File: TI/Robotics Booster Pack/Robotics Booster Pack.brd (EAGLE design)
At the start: 68.6 x 76.2 mm, 115 parts, among them J1 1X2.PTS, U1 TS3A44159.RGT, U10 74LVTH125.RGY, U11 SCHA4B0400, U12 BLUETOOTH-RN41", U13 XBEE-1XBEE-1_LOCK, U14 TPS5450, U15 TPS715XX.DCK, U16 TPS62152.RGT, U3 DRV8800, U4 DRV8800, U5 DRV8800, U6 DRV8800, U7 PCA9557.RGV, U8 MPU-6050, U9 INA220.DGS

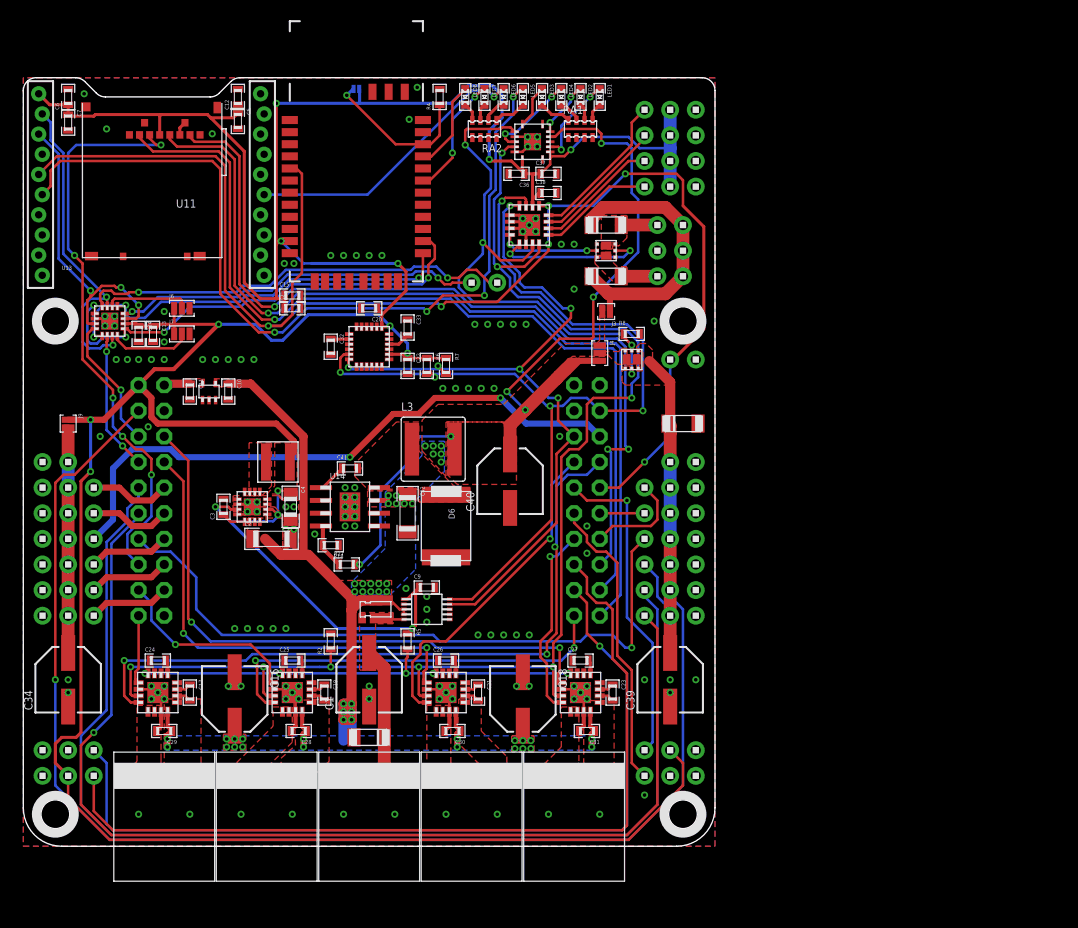
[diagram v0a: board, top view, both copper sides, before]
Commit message: Began starting on v2.1 Removed: Bluetooth Module, Servo Enable IC, Buffer IC. Corrected Motor PWM/IO signals issue Centered power ICs
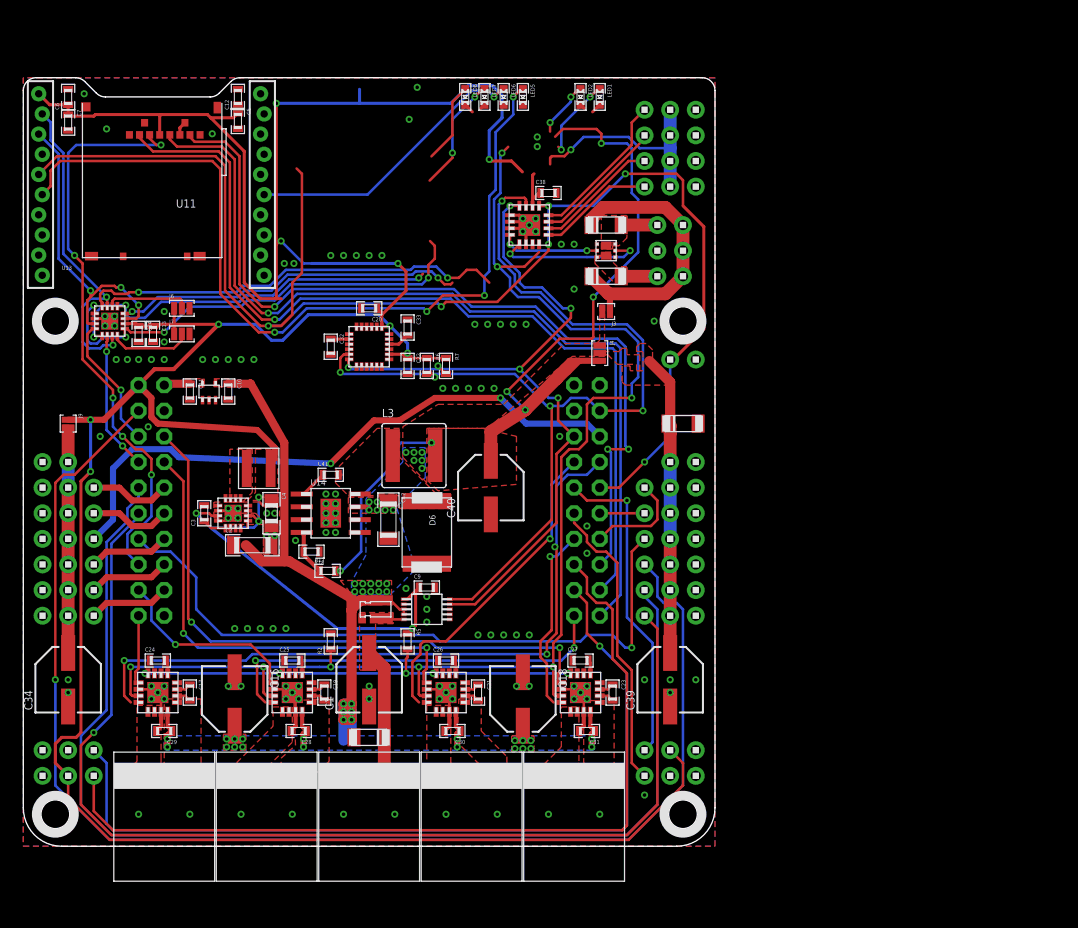
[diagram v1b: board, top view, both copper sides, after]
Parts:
- removed C15, C37: 1uF, standardparts:0603
- removed C36, C8: .1uF, standardparts:0603
- removed J2: (no value), solderjumper:2.MED
- removed LED3, LED4: (no value), standardparts:0603.LED
- removed Q2: (no value), fairchild:MICROFET.2X2
- removed R4: 1k, standardparts:0603
- removed R8: 10k, standardparts:0603
- removed RA1, RA2: 1k, resistorarray:0603.4.C
- removed U$15: 1X2, headers(.1in):1X2
- removed U10: 74LVTH125.RGY, packages(ti):RGY.14
- removed U12: BLUETOOTH-RN41", SparkFun-RF:RN41
- moved C42 2.01 mm to (36.2, 32.4)
- moved R17 2.01 mm to (30.2, 27.3)
- moved C3 2.01 mm to (17.9, 33.0)
- moved C4 2.01 mm to (24.6, 33.0)
- moved C40 2.01 mm to (46.4, 35.6)
- moved L1 2.01 mm to (23.3, 37.5)
- moved L3 2.01 mm to (38.7, 38.7)
- moved R18 2.01 mm to (28.6, 29.2)
- moved U16 2.01 mm to (20.8, 33.0)
- moved C41 2.01 mm to (30.5, 36.8)
- moved C2 2.01 mm to (22.7, 29.8)
- moved U14 2.01 mm to (30.5, 33.0)
- moved D6 2.01 mm to (40.0, 31.1)
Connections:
- removed net BT.RESET: J2.1, R4.1, U12.22
- removed net N$12: LED4.P$2, RA1.4
- removed net N$15: LED6.P$2, RA2.3
- removed net N$16: J4.2, Q2.3, Q2.6, Q2.PAD@1, Q2.PAD@2
- removed net N$17: LED5.P$2, RA2.1
- removed net N$26: LED3.P$2, RA1.2
- removed net N$32: LED3.P$1, U10.8
- removed net N$6: LED4.P$1, U10.11
- removed net SRVO.EN: Q2.2, Q2.5, R8.1, U10.9, U7.7
- new net VDD: J4.2
- net !RST: no longer U12.5
- net 3.3V: no longer C15.1, C36.1, C37.1, C8.1, J2.2, U10.14, U10.2, U12.11
- net 5.0V: no longer U10.5
- net BT.CONNECT: no longer U12.21
- net BT.RXI: no longer U12.14
- net BT.STATUS: no longer U12.19
- net BT.TXO: no longer U12.13
- net GND: no longer C15.2, C36.2, C37.2, C8.2, R4.2, R8.2, RA1.1, RA1.3, RA1.5, RA1.7, RA2.2, RA2.4, RA2.6, RA2.8, U10.1, U10.10, U10.13, U10.4, U10.7, U10.PAD, U12.1, U12.12, U12.25, U12.27, U12.28, U12.29
- net M.EN: no longer U10.12, U7.8
- net M0.DIR: now also U5.1; no longer U5.4
- net M0.SPD: now also U5.4; no longer U5.1
- net M1.DIR: now also U6.1; no longer U6.4
- net M1.SPD: now also U6.4; no longer U6.1
- net M2.DIR: now also U3.1; no longer U3.4
- net M2.SPD: now also U3.4; no longer U3.1
- net M3.DIR: now also U4.1; no longer U4.4
- net M3.SPD: now also U4.4; no longer U4.1
- net N$10: no longer U10.6
- net N$11: no longer U10.3
- net N$14: no longer RA2.7
- net N$5: no longer RA1.8
- net N$8: no longer RA1.6
- net N$9: no longer RA2.5
- net UART0.RXI: no longer U$15.2
- net UART0.TXO: no longer U$15.1
- net VSERVO: no longer Q2.1, Q2.4
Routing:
- net SRVO.EN: track 54.7 -> 0.00 mm, vias 4 -> 0
- net BT.RESET: track 15.6 -> 0.00 mm, vias 1 -> 0
- net N$6: track 8.94 -> 0.00 mm, vias 2 -> 0
- net 3.3V: track 388.9 -> 380.3 mm
- net N$32: track 4.27 -> 0.00 mm
- net N$26: track 3.26 -> 0.00 mm
- net N$17: track 3.25 -> 0.00 mm
- net GND: track 40.4 -> 37.6 mm, vias 132 -> 130
- net N$15: track 2.44 -> 0.00 mm
- net N$12: track 2.35 -> 0.00 mm
- net BT.TXO: track 42.0 -> 39.9 mm
- net UART0.TXO: track 36.7 -> 34.8 mm
- net M.EN: track 133.0 -> 131.6 mm
- net 5.0V: track 83.0 -> 84.5 mm
- net N$9: track 1.72 -> 0.57 mm
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
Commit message: Let the carnage that shall be known as v3 begin!
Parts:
- removed C10, C13: .1uF, standardparts:0603
- removed C11, C14: 1uF, standardparts:0603
- removed D5: CDBMT2100-HF, comchip:SOD-123H
- removed H11, H12: 1X4, headers(.1in):1X4
- removed H17, H18, H19, H20, J1: 1X2.PTS, phoenixcontact:PTS.PLUG
- removed J6, J7: (no value), solderjumper:3.LRG
- removed J9: (no value), solderjumper:2.LRG.PASTE
- removed R2: 10k, standardparts:0603
- removed U$11, U$14: HOLE.4MM, screw_holes:4MM
- removed U1: TS3A44159.RGT, packages(ti):RGT.16
- removed U15: TPS715XX.DCK, packages(ti):DCK
- added H8: 1X4.182440000, weidmuller:1824440000
- H1, H2, H4, H5: value 1X7 -> 1X6; device headers(.1in):1X7 -> headers(.1in):1X6
- H10: value 1X4 -> 1X4.182440000; device headers(.1in):1X4 -> weidmuller:1824440000
- moved C6 107.7 mm to (89.5, 8.26), turned to 270 degrees
- moved C7 104.7 mm to (89.5, 10.8), turned to 90 degrees
- moved U11 84.7 mm to (74.3, 8.89), turned to 0 degrees
- moved C12 83.7 mm to (72.7, 8.26), turned to 270 degrees
- moved C5 80.0 mm to (72.7, 10.6), turned to 90 degrees
- moved U13 73.6 mm to (81.3, 27.9), turned to 180 degrees
- moved C23 58.2 mm to (31.1, 66.7), turned to 0 degrees
- moved C31 56.7 mm to (34.9, 64.1), turned to 270 degrees
- moved U4 54.0 mm to (31.1, 63.5), turned to 90 degrees
- moved C27 52.7 mm to (27.9, 63.5), turned to 90 degrees
- moved C18 46.7 mm to (31.8, 57.8), turned to 0 degrees
- moved C40 46.6 mm to (5.08, 57.1), turned to 270 degrees
- moved LED1 45.1 mm to (85.7, 39.4)
- moved LED2 45.1 mm to (83.8, 39.4)
- moved LED5 45.1 mm to (78.1, 39.4)
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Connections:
- removed net BT.CONNECT: LED8.P$1
- removed net BT.RXI: U1.13, U1.5
- removed net BT.STATUS: LED7.P$1
- removed net BT.TXO: U1.1, U1.9
- removed net IO0: H12.1, U7.12
- removed net IO1: H12.2, U7.11
- removed net IO2: H12.3, U7.10
- removed net IO3: H12.4, U7.9
- removed net M.EN: R2.1, U3.3, U4.3, U5.3, U6.3
- removed net N$2: J6.2, U1.2
- removed net N$3: J7.2, U1.12
- removed net UART0.RXI: U1.4
- removed net UART0.TXO: U1.16
- removed net VBUS: C11.1, U$8.VBUS, U15.5
- new net IMU.INT: U7.5, U8.12
- new net M0.EN: U5.3, U7.9
- new net M1.EN: U6.3, U7.10
- new net M2.EN: U3.3, U7.11
- new net M3.EN: U4.3, U7.12
- new net XBEE.CONNECTED: U13.17, U7.4
- net 3.3V: no longer C13.1, C14.1, H11.1, H11.2, H11.3, H11.4, J6.1, J7.1, J9.1, U1.14
- net 5.0V: now also U$8.VBUS
- net FET0.G: now also U7.7; no longer U7.4
- net FET1.G: now also U7.8; no longer U7.5
- net GND: no longer C10.2, C11.2, C13.2, C14.2, D5.2, H1.7, H10.1, H10.2, H10.3, H10.4, H4.7, J1.2, J6.3, J7.3, R2.2, U1.6, U1.PAD, U15.2
- net M0+: now also H8.1@1, H8.1@2; no longer H17.1
- net M0-: now also H8.2@1, H8.2@2; no longer H17.2
- net M0.DIR: now also U$8.PC4; no longer U$8.PF0
- net M1+: now also H8.3@1, H8.3@2; no longer H18.1
- net M1-: now also H8.4@1, H8.4@2; no longer H18.2
- net M1.DIR: now also U$8.PC7; no longer U$8.PF4
- net M2+: now also H10.1@1, H10.1@2; no longer H19.1
- net M2-: now also H10.2@1, H10.2@2; no longer H19.2
- net M2.DIR: now also U$8.PF0; no longer U$8.PC4
- net M3+: now also H10.3@1, H10.3@2; no longer H20.1
- net M3-: now also H10.4@1, H10.4@2; no longer H20.2
- net M3.DIR: now also U$8.PF4; no longer U$8.PC7
- net N$22: no longer J1.1
- net N$4: no longer H5.7, J9.2
- net UART1.RXI: no longer U1.8
- net UART1.TXO: no longer U1.10
- net VBAT: no longer C10.1, U15.4
- net VSERVO: no longer D5.1, H2.7
- net XBEE.RXI: no longer U1.11, U1.3
- net XBEE.TXO: no longer U1.15, U1.7
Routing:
- net 3.3V: track 380.3 -> 3.81 mm, vias 14 -> 0
- net !RST: track 144.0 -> 0.00 mm, vias 6 -> 0
- net SVRO3: track 132.1 -> 0.00 mm, vias 1 -> 0
- net M.EN: track 131.6 -> 0.00 mm, vias 8 -> 0
- net SVRO4: track 115.2 -> 0.00 mm
- net SVRO5: track 110.2 -> 0.00 mm, vias 1 -> 0
- net I2C.SCL: track 95.1 -> 0.00 mm, vias 5 -> 0
- net SPI.SCLK: track 90.0 -> 0.00 mm, vias 1 -> 0
- net SPI.!CS: track 89.6 -> 0.00 mm, vias 1 -> 0
- net QEI0.A: track 85.9 -> 0.00 mm
- net QEI0.B: track 85.4 -> 0.00 mm, vias 1 -> 0
- net SPI.MISO: track 85.3 -> 0.00 mm, vias 3 -> 0
- net XBEE.RSSI: track 84.3 -> 0.00 mm, vias 4 -> 0
- net VBAT: track 81.8 -> 1.20 mm, vias 48 -> 12
- net I2C.SDA: track 75.9 -> 0.00 mm, vias 6 -> 0
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- added copper zone on layer 16, net 3.3V
- added copper zone on layer 16, net N$1
- removed copper zone on layer 1, net 3.3V
- removed copper zone on layer 1, net 5.0V
- removed copper zone on layer 1, net M0+
- removed copper zone on layer 1, net M0-
- removed copper zone on layer 1, net M1+
- removed copper zone on layer 1, net M1-
- removed copper zone on layer 1, net M2+
- removed copper zone on layer 1, net M2-
- removed copper zone on layer 1, net M3+
- removed copper zone on layer 1, net M3-
- removed copper zone on layer 1, net N$1
- removed copper zone on layer 1, net N$16
- removed copper zone on layer 1, net N$22
- removed copper zone on layer 1, net VBUS
- removed copper zone on layer 1, net VSERVO
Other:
- board size 68.6 x 76.2 mm -> 68.6 x 67.3 mm
- board text removed: "3.3v"
- board text removed: "5V"
- board text removed: "5v"
- board text removed: "ADC"
- board text removed: "Associate"
- board text removed: "BT"
- board text removed: "Connect"
- board text removed: "ENC 0"
- board text removed: "ENC 1"
- board text removed: "GPIO"
- board text removed: "M0"
- board text removed: "M1"
- board text removed: "M2"
- board text removed: "M3"
- board text removed: "Motors ON"
- board text removed: "RSSI"
- board text removed: "SERVO"
- board text removed: "Servos ON"
- board text removed: "Status"
- board text removed: "UART0"
- board text removed: "UART1"
- board text removed: "VBAT"
- board text removed: "VSRVO"
- board text removed: "VSVRO"
- board text removed: "XBee"

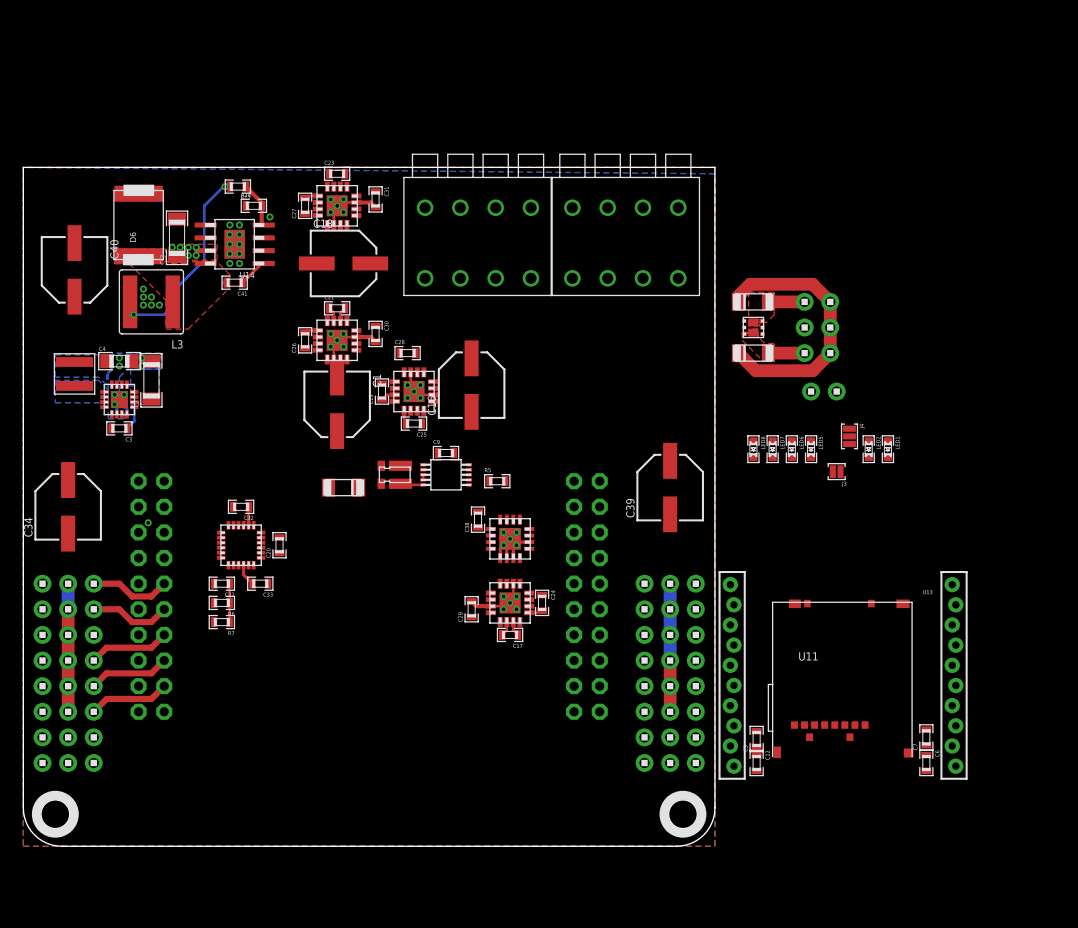
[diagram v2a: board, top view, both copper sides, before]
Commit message: Continued working on RBP v3 Using TPS62177 for 3.3v regulator circuit, new Vin headers, moving things around.
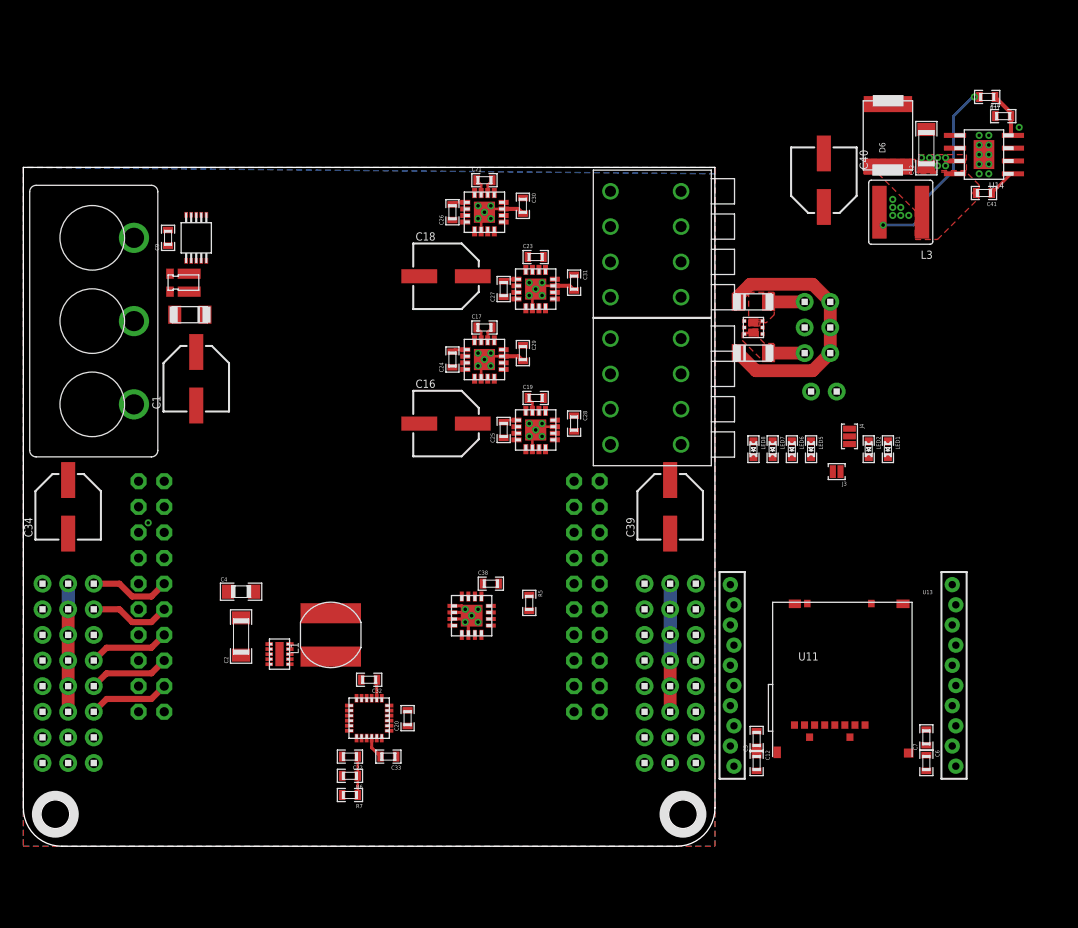
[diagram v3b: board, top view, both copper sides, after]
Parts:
- removed C3: 330nF, standardparts:0603
- removed U16: TPS62152.RGT, packages(ti):RGT.16
- added H11: 1X3.4DB, te-connectivity:4DB-P108-02
- added U1: TPS62177.DQC, packages(ti):DQC
- C2: value 10uF -> 2.2uF
- L1: value 2.2uH -> 10uH; device coilcraft:XAL4020 -> bourns:SRN6045
- moved C40 74.8 mm to (79.4, 66.0)
- moved C41 74.8 mm to (95.2, 64.8)
- moved C42 74.8 mm to (89.5, 69.2)
- moved L3 74.8 mm to (87.0, 62.9)
- moved R18 74.8 mm to (97.2, 72.4)
- moved U14 74.8 mm to (95.2, 68.6)
- moved D6 74.8 mm to (85.7, 70.5)
- moved R17 74.8 mm to (95.6, 74.3)
- moved L1 36.3 mm to (30.5, 21.0)
- moved C9 34.9 mm to (14.4, 60.3), turned to 90 degrees
- moved U9 34.1 mm to (17.1, 60.3), turned to 180 degrees
- moved C17 30.6 mm to (45.7, 51.4), turned to 0 degrees
- moved R1 28.3 mm to (15.9, 55.9)
- moved C2 26.9 mm to (21.6, 20.8)
- moved C29 25.9 mm to (49.5, 48.9), turned to 270 degrees
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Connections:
- removed net N$23: C3.1, U16.9
- net 3.3V: now also U1.10, U1.8; no longer U16.14, U16.7
- net GND: now also H11.1, U1.1, U1.5, U1.6, U1.PAD; no longer C3.2, U16.15, U16.16, U16.5, U16.6, U16.8, U16.PAD
- net N$1: now also U1.9; no longer U16.1, U16.2, U16.3
- net N$22: now also H11.2
- net VBAT: now also H11.3, U1.2, U1.3; no longer U16.10, U16.11, U16.12, U16.13
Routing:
- net GND: track 32.5 -> 29.5 mm, vias 44 -> 37
- net N$23: track 2.40 -> 0.00 mm
- net N$22: track 2.27 -> 0.00 mm
- net VBAT: track 1.20 -> 0.00 mm
- removed copper zone on layer 16, net 3.3V
- removed copper zone on layer 16, net N$1
- removed copper zone on layer 16, net VBAT
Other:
- board text removed: "!RST"
- board text removed: "GND"

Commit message: COntinuing work on RBP v3 Added smd headers to replace Launchpad throguh hole headers (more routing space on the bottom) Moved around motor controllers -n- stuff.
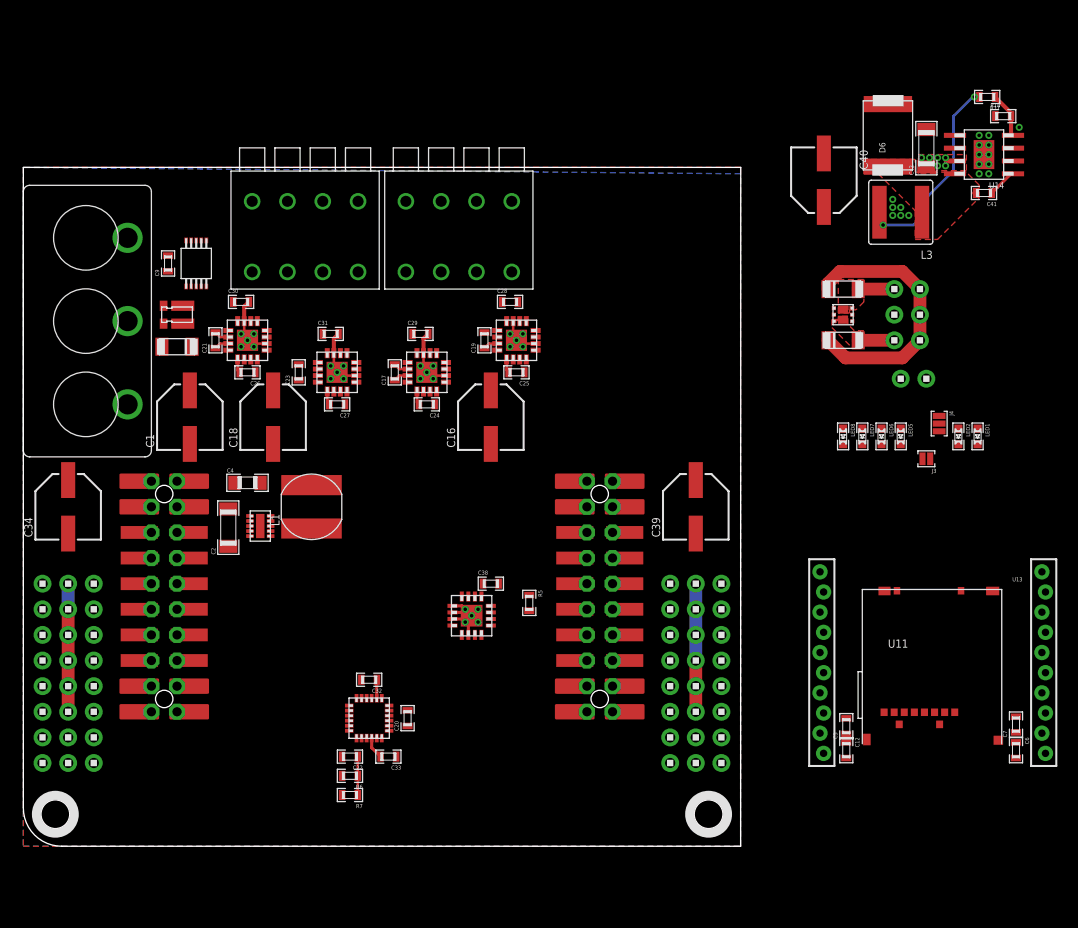
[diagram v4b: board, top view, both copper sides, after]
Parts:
- added H12, H15: 2X10.TSM-D-A, headers(.1in)(samtec):TSM-110-XX-XXX-DV-A
- moved C21 31.0 mm to (19.1, 50.2), turned to 90 degrees
- moved C30 29.5 mm to (21.6, 54.0), turned to 0 degrees
- moved H10 28.9 mm to (27.9, 55.2), turned to 0 degrees
- moved U3 26.7 mm to (22.2, 50.2), turned to 180 degrees
- moved C23 26.1 mm to (27.3, 47.0), turned to 90 degrees
- moved C26 25.8 mm to (22.2, 47.0), turned to 180 degrees
- moved C31 24.7 mm to (30.5, 50.8), turned to 0 degrees
- moved C18 22.1 mm to (24.8, 42.5), turned to 90 degrees
- moved U4 21.3 mm to (31.1, 47.0), turned to 180 degrees
- moved C27 20.1 mm to (31.1, 43.8), turned to 180 degrees
- moved H8 16.8 mm to (43.2, 55.2), turned to 0 degrees
- moved C28 13.6 mm to (48.3, 54.0), turned to 0 degrees
- moved L1 12.8 mm to (28.6, 33.7)
- moved U1 12.8 mm to (23.5, 31.8)
- moved C2 10.9 mm to (20.3, 31.6)
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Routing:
- net AD5: track 8.04 -> 0.00 mm
- net AD4: track 8.04 -> 0.00 mm
- net AD3: track 8.04 -> 0.00 mm
- net AD1: track 8.04 -> 0.00 mm
- net AD0: track 8.04 -> 0.00 mm
- net GND: vias 37 -> 36
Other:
- board size 68.6 x 67.3 mm -> 71.1 x 67.3 mm
